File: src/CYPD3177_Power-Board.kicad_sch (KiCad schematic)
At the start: 48 parts, among them J1 Conn_01x06, J2 USB4125-GF-A, J3 Conn_01x03, J4 Conn_01x03, J5 Conn_01x03, Q1 IRF9358PbF, Q2 BSL308PE, Q3 NTR4503N, U1 CYPD3177-24LQXQx

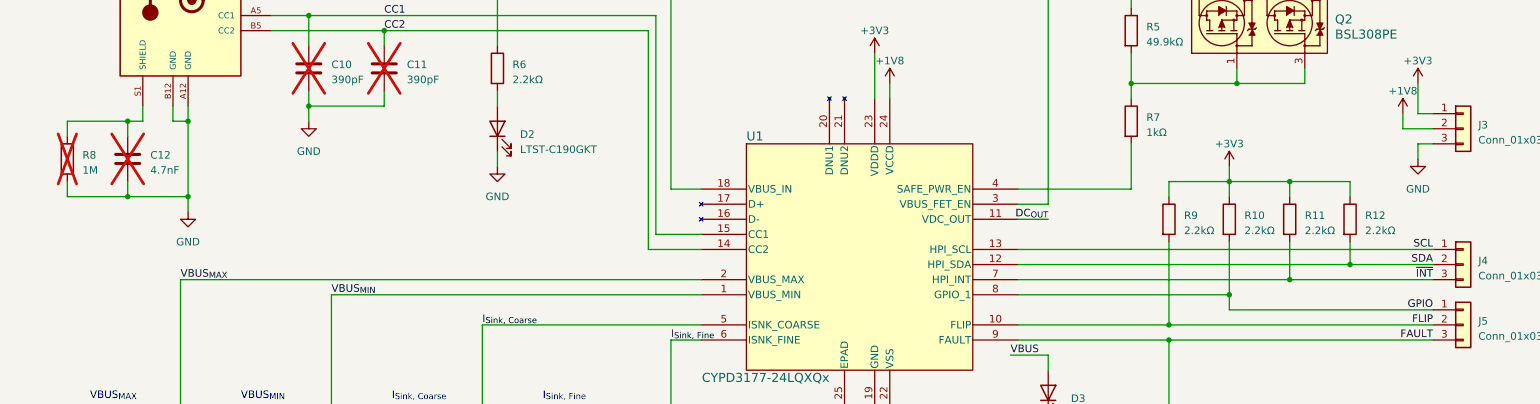
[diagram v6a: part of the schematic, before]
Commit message: Mod: PCB, placed components, draw board shape and placed a few traces
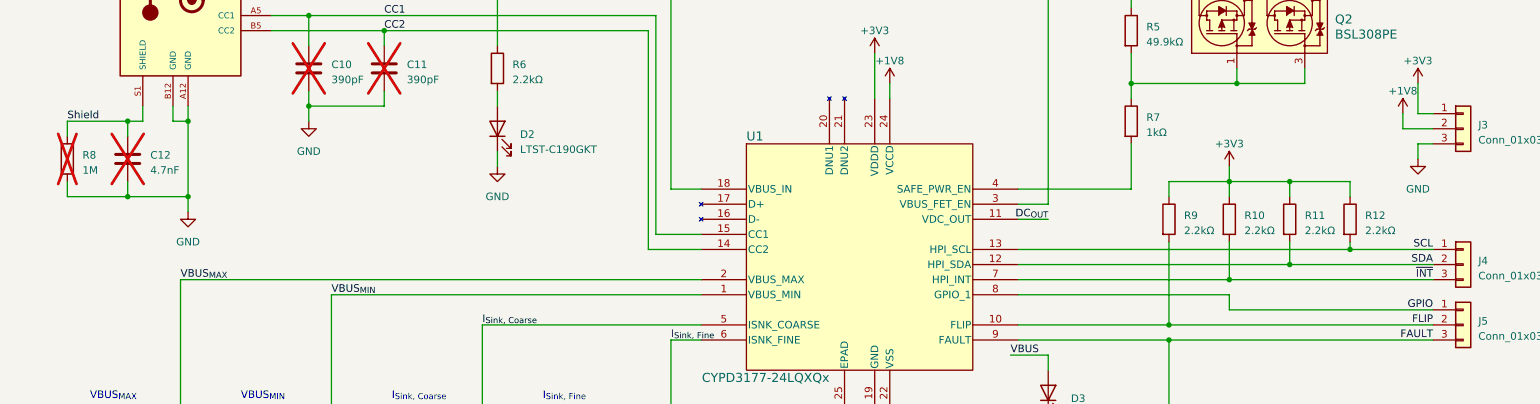
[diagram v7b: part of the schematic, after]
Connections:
- net GPIO: no longer R10.2
- net SCL: now also R12.2
- net SDA: now also R11.2; no longer R12.2
- net ~{INT}: now also R10.2; no longer R11.2
- net Shield: now reaches C12.1, J2.S1 (SHIELD), R8.1
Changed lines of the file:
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@@
   (junction (at 217.17 121.92) (diameter 0) (color 0 0 0 0)
   )
-  (junction (at 247.65 111.76) (diameter 0) (color 0 0 0 0)
-  )
   (junction (at 85.09 72.39) (diameter 0) (color 0 0 0 0)
   )
@@
   (junction (at 171.45 49.53) (diameter 0) (color 0 0 0 0)
   )
+  (junction (at 247.65 109.22) (diameter 0) (color 0 0 0 0)
+  )
+  (junction (at 237.49 111.76) (diameter 0) (color 0 0 0 0)
+  )
   (junction (at 256.54 26.67) (diameter 0) (color 0 0 0 0)
   )
-  (junction (at 237.49 114.3) (diameter 0) (color 0 0 0 0)
-  )
   (junction (at 259.08 19.05) (diameter 0) (color 0 0 0 0)
   )
@@
   (junction (at 104.14 62.23) (diameter 0) (color 0 0 0 0)
   )
-  (junction (at 227.33 116.84) (diameter 0) (color 0 0 0 0)
-  )
   (junction (at 133.35 62.23) (diameter 0) (color 0 0 0 0)
   )
@@
   (junction (at 196.85 49.53) (diameter 0) (color 0 0 0 0)
   )
+  (junction (at 227.33 114.3) (diameter 0) (color 0 0 0 0)
+  )
   (junction (at 133.35 44.45) (diameter 0) (color 0 0 0 0)
   )
@@
     (stroke (width 0) (type default))
   )
-  (wire (pts (xy 247.65 111.76) (xy 261.62 111.76))
-    (stroke (width 0) (type default))
-  )
   (wire (pts (xy 114.3 153.67) (xy 114.3 156.21))
     (stroke (width 0) (type default))
@@
     (stroke (width 0) (type default))
   )
-  (wire (pts (xy 191.77 109.22) (xy 261.62 109.22))
+  (wire (pts (xy 191.77 109.22) (xy 247.65 109.22))
     (stroke (width 0) (type default))
   )
@@
     (stroke (width 0) (type default))
   )
+  (wire (pts (xy 237.49 111.76) (xy 261.62 111.76))
+    (stroke (width 0) (type default))
+  )
   (wire (pts (xy 256.54 88.9) (xy 256.54 86.36))
     (stroke (width 0) (type default))
@@
     (stroke (width 0) (type default))
   )
-  (wire (pts (xy 237.49 107.95) (xy 237.49 114.3))
-    (stroke (width 0) (type default))
-  )
   (wire (pts (xy 38.1 151.13) (xy 38.1 153.67))
     (stroke (width 0) (type default))
@@
     (stroke (width 0) (type default))
   )
-  (wire (pts (xy 191.77 111.76) (xy 247.65 111.76))
-    (stroke (width 0) (type default))
-  )
-  (wire (pts (xy 247.65 107.95) (xy 247.65 111.76))
+  (wire (pts (xy 191.77 111.76) (xy 237.49 111.76))
     (stroke (width 0) (type default))
   )
@@
     (stroke (width 0) (type default))
   )
-  (wire (pts (xy 227.33 107.95) (xy 227.33 116.84))
-    (stroke (width 0) (type default))
-  )
   (wire (pts (xy 41.91 87.63) (xy 44.45 87.63))
     (stroke (width 0) (type default))
@@
     (stroke (width 0) (type default))
   )
+  (wire (pts (xy 247.65 109.22) (xy 261.62 109.22))
+    (stroke (width 0) (type default))
+  )
   (wire (pts (xy 256.54 26.67) (xy 261.62 26.67))
     (stroke (width 0) (type default))
@@
     (stroke (width 0) (type default))
   )
+  (wire (pts (xy 237.49 107.95) (xy 237.49 111.76))
+    (stroke (width 0) (type default))
+  )
   (wire (pts (xy 72.39 85.09) (xy 85.09 85.09))
     (stroke (width 0) (type default))
@@
     (stroke (width 0) (type default))
   )
+  (wire (pts (xy 247.65 107.95) (xy 247.65 109.22))
+    (stroke (width 0) (type default))
+  )
+  (wire (pts (xy 227.33 107.95) (xy 227.33 114.3))
+    (stroke (width 0) (type default))
+  )
   (wire (pts (xy 171.45 19.05) (xy 171.45 34.29))
     (stroke (width 0) (type default))
@@
     (stroke (width 0) (type default))
   )
-  (wire (pts (xy 237.49 114.3) (xy 261.62 114.3))
-    (stroke (width 0) (type default))
-  )
   (wire (pts (xy 222.25 19.05) (xy 259.08 19.05))
     (stroke (width 0) (type default))
@@
     (stroke (width 0) (type default))
   )
+  (wire (pts (xy 227.33 114.3) (xy 261.62 114.3))
+    (stroke (width 0) (type default))
+  )
   (wire (pts (xy 38.1 140.97) (xy 38.1 143.51))
     (stroke (width 0) (type default))
@@
     (stroke (width 0) (type default))
   )
-  (wire (pts (xy 191.77 114.3) (xy 237.49 114.3))
+  (wire (pts (xy 191.77 114.3) (xy 227.33 114.3))
     (stroke (width 0) (type default))
   )
@@
     (effects (font (size 1.27 1.27)) (justify right bottom))
   )
+  (label "Shield" (at 31.75 87.63 0) (fields_autoplaced)
+    (effects (font (size 1.27 1.27)) (justify left bottom))
+  )
   (label "FET_{SRC}" (at 80.01 25.4 0) (fields_autoplaced)

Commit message: Add: Parts from LCSC
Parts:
- D3: value LTST-C190EKT -> LTST-C190EKT
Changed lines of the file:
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@@
       (effects (font (size 1.27 1.27)) (justify right))
     )
-    (property "Value" "LTST-C190EKT\n" (at 200.66 136.8425 90)
+    (property "Value" "LTST-C190EKT" (at 200.66 136.8425 90)
       (effects (font (size 1.27 1.27)) (justify right))
     )
